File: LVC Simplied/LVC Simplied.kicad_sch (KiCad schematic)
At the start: 14 parts, among them Q1 IRF9540N, U1 TL431A, U3 LM393

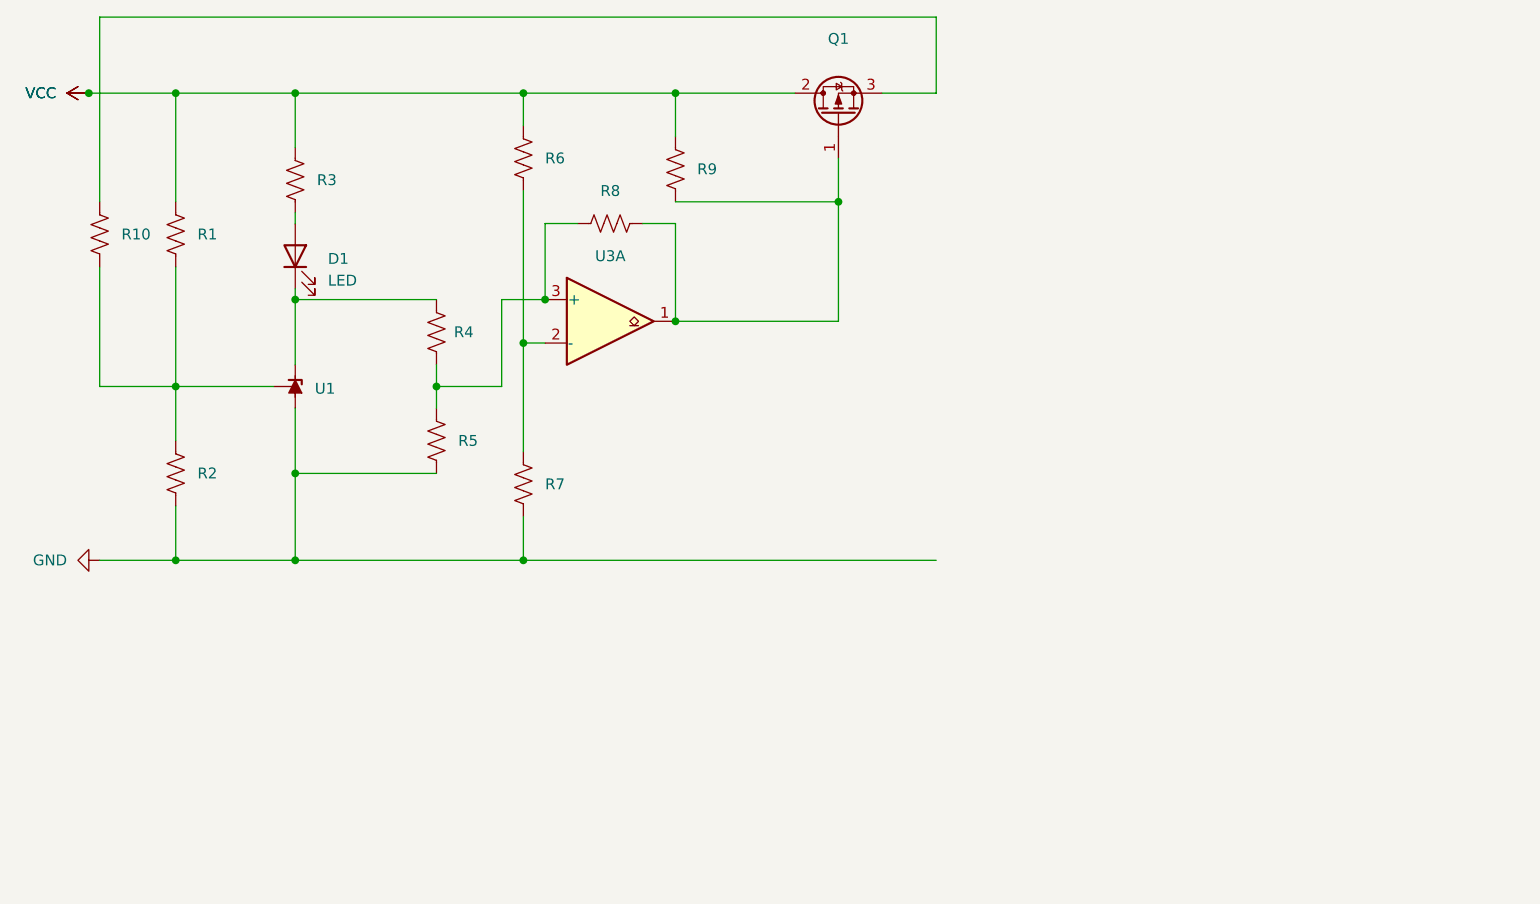
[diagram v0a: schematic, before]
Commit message: LVC Simplified Added
Refining the idea of a simplified LVC circuit and providing two alternatives to doing so.

- High Side Switch
- Low Side Switch (preferred)
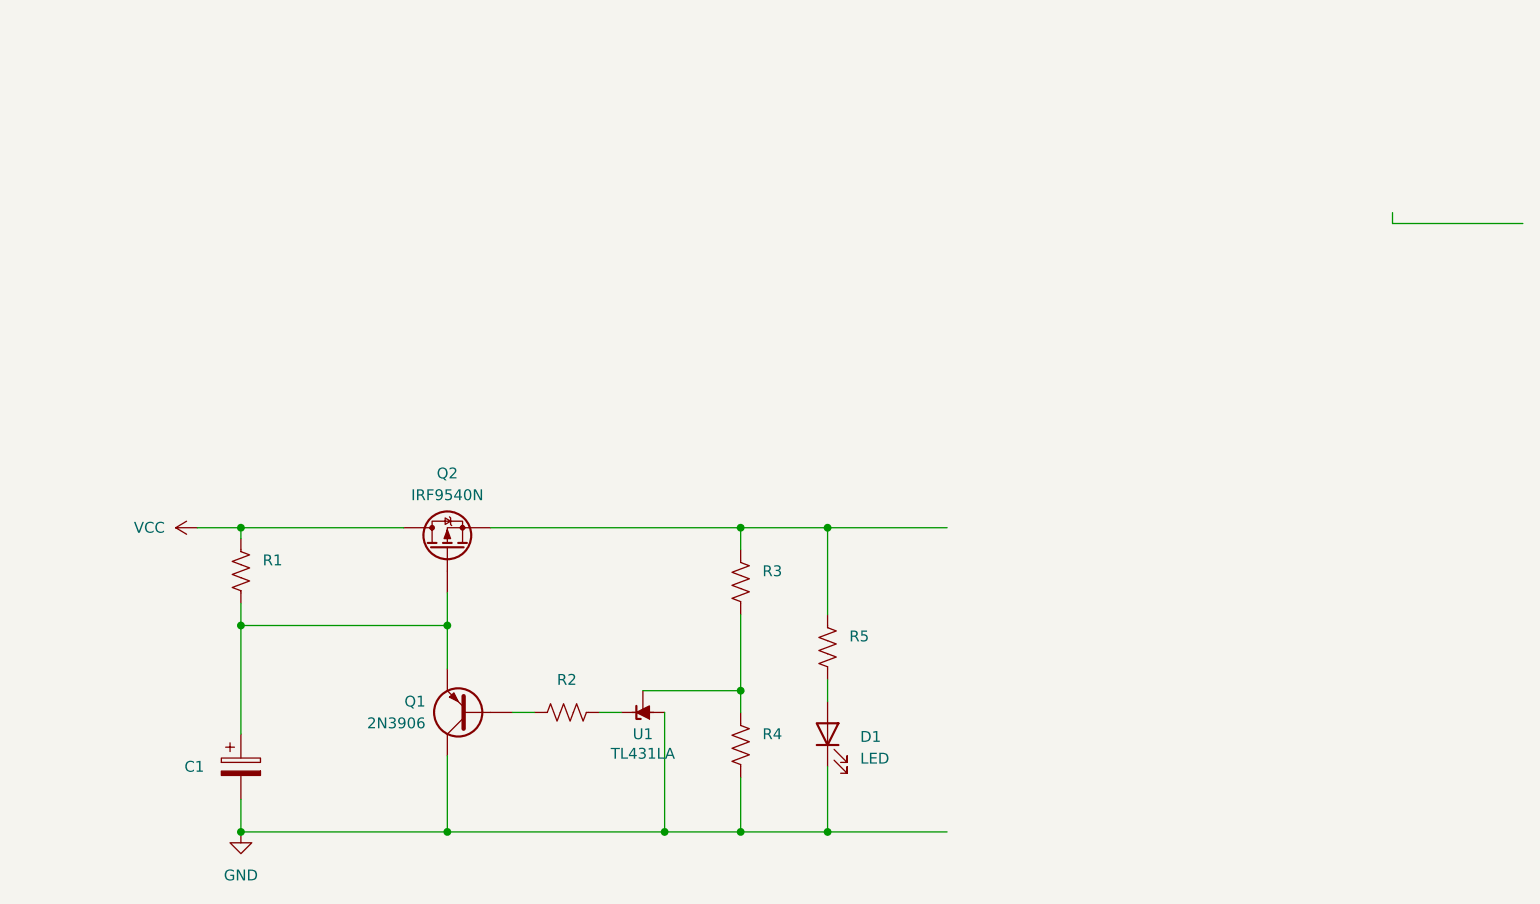
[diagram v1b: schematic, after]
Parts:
- removed Q1: IRF9540N, Package_TO_SOT_THT:TO-220-3_Vertical, symbol Transistor_FET:IRF9540N
- removed R10, R6, R7, R8, R9: R_US, symbol Device:R_US
- removed U1: TL431A, Package_TO_SOT_SMD:SOT-23, symbol Reference_Voltage:TL431DBZ
- removed U3: LM393, symbol Comparator:LM393
- added C1: C_Polarized, symbol Device:C_Polarized
- added Q1: 2N3906, Package_TO_SOT_THT:TO-92_Inline, symbol Transistor_BJT:2N3906
- added Q2: IRF9540N, Package_TO_SOT_THT:TO-220-3_Vertical, symbol Transistor_FET:IRF9540N
- added U1: TL431LA, Package_TO_SOT_THT:TO-92_Inline, symbol Reference_Voltage:TL431LP
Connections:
- net GND: now also D1.1 (K), R4.2, C1.2, Q1.3 (C), U1.2 (A); no longer R2.2, R5.2
- net VCC: now also Q2.2 (D); no longer R3.1
- net at R5.1: now also R3.1, Q2.3 (S); no longer R4.2
- net at R4.1: now also R3.2, U1.1 (REF); no longer D1.1 (K)
- net at R1.2: now also C1.1, Q1.1 (E), Q2.1 (G); no longer R2.1
- net at D1.2 (A): now also R5.2; no longer R3.2
- new net: Q1.2 (B), R2.1
- new net: R2.2, U1.3 (K)

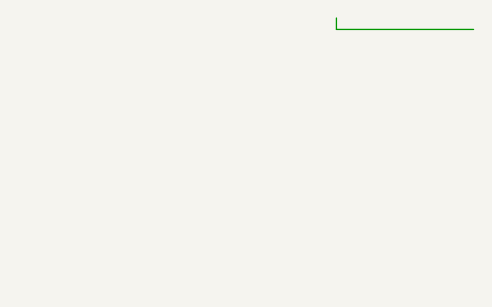
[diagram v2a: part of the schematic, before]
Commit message: LVC Low Side V2
Another version of a low side switch is provided that has the following features:

- Way lower power consumption
- A blinking LED that provides a visual indication that the power is past the cutt_off point
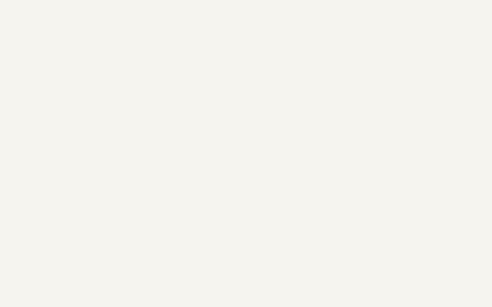
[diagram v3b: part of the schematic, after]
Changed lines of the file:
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@@
-	(wire
-		(pts
-			(xy 191.77 49.53) (xy 191.77 50.8)
-		)
-		(stroke
-			(width 0)
-			(type default)
-		)
-	)
-	(wire
-		(pts
-			(xy 191.77 50.8) (xy 207.01 50.8)
-		)
-		(stroke
-			(width 0)
-			(type default)
-		)
-	)
 	(wire
 		(pts
